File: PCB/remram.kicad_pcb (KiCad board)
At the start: 4 copper layers, 140 x 103 mm, 208 parts, among them J1 4DB-P108-06, J10 70543-0002, J11 Conn_02x13_Odd_Even, J12 70543-0002, J13 70543-0002, J14 70543-0002, J15 70543-0003, J16 62201021121, J17 70543-0001, J18 70543-0001, J19 70543-0001, J2 039531-1002, J20 70543-0003, J21 70543-0003, J22 70543-0003, J23 70543-0003, J3 70543-0002, J4 70543-0002, J5 70543-0002, J6 67068-8000, J7 Conn_02x05, J8 Conn_02x05, J9 70543-0002, Q1 PSMN1R8-40YLC,115, Q2 BUK9840-55, Q3 PSMN1R8-40YLC,115, Q4 BUK9840-55, SW1 OS102011MA1QN1, SW2 PTS645VL39-2, U1 TPS54308, U2 AP2112K-3.3TRG1, U3 ADUM4160, U4 STM32F765VIT6, U5 TMC2130-TA, U6 TMC2130-TA, U7 TMC2130-TA, U8 TMC2130-TA, Y1 TSX-3225 24.0000MF15X-AC3

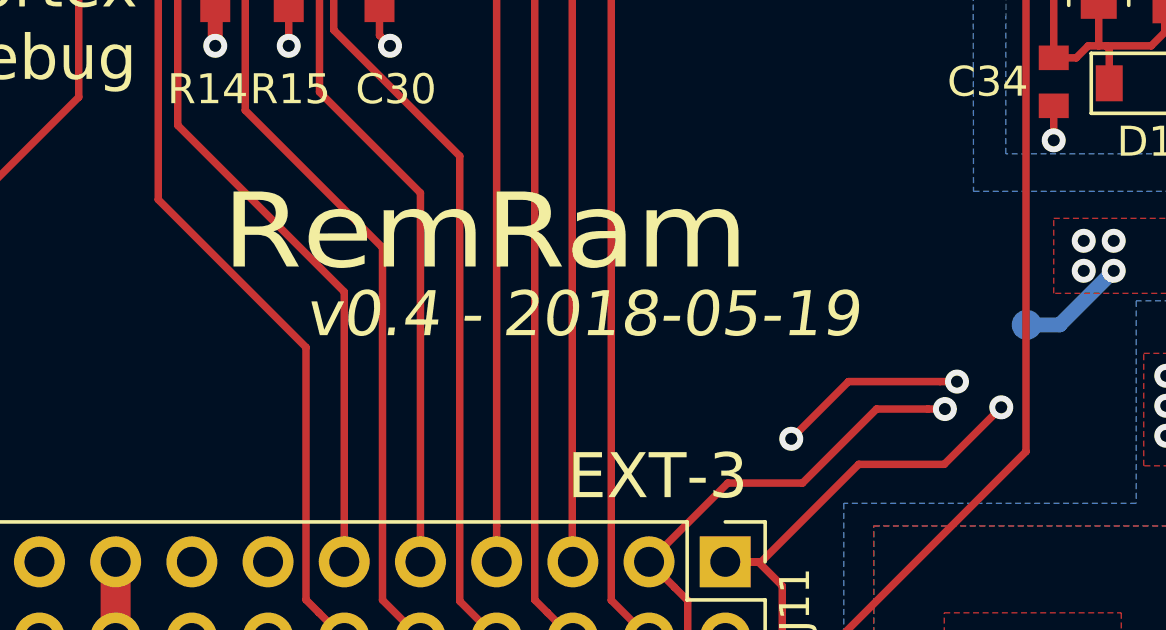
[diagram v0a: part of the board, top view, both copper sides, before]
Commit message: Changed LED to sane values. Updated diodes. v0.5.
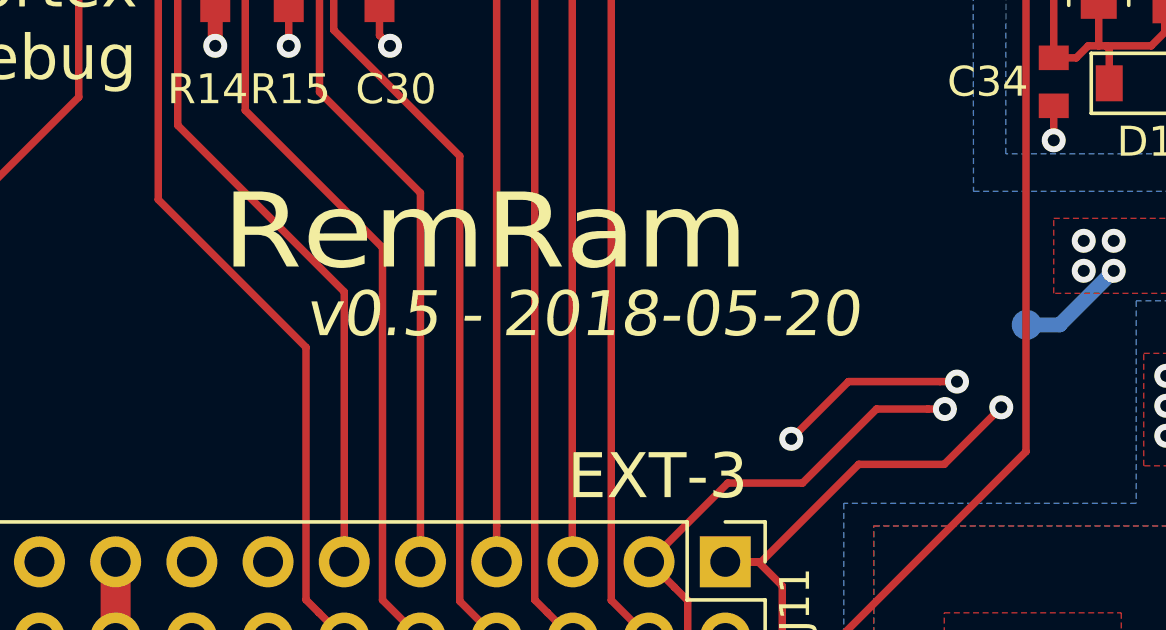
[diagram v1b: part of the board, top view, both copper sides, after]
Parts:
- D5, D7: value SK310A-TP -> SK310A-LTP
- R20, R3: value 68 -> 1k
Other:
- board text added: "v0.5 - 2018-05-20"
- board text removed: "v0.4 - 2018-05-19"
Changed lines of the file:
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@@
       (effects (font (size 1 1) (thickness 0.15)))
     )
-    (fp_text value 68 (at 0 1.45 180) (layer F.Fab)
+    (fp_text value 1k (at 0 1.45 180) (layer F.Fab)
       (effects (font (size 1 1) (thickness 0.15)))
     )
@@
       (effects (font (size 1 1) (thickness 0.15)))
     )
-    (fp_text value SK310A-TP (at 0 2.6 90) (layer F.Fab)
+    (fp_text value SK310A-LTP (at 0 2.6 90) (layer F.Fab)
       (effects (font (size 1 1) (thickness 0.15)))
     )
@@
       (effects (font (size 1 1) (thickness 0.15)))
     )
-    (fp_text value SK310A-TP (at 0 2.6 90) (layer F.Fab)
+    (fp_text value SK310A-LTP (at 0 2.6 90) (layer F.Fab)
       (effects (font (size 1 1) (thickness 0.15)))
     )
@@
       (effects (font (size 1 1) (thickness 0.15)))
     )
-    (fp_text value 68 (at 0 1.45 270) (layer F.Fab)
+    (fp_text value 1k (at 0 1.45 270) (layer F.Fab)
       (effects (font (size 1 1) (thickness 0.15)))
     )
@@
     (arrow2b (pts (xy 202.199068 149.769839) (xy 201.07246 150.356059)))
   )
-  (gr_text "v0.4 - 2018-05-19" (at 134 116) (layer F.SilkS)
+  (gr_text "v0.5 - 2018-05-20" (at 134 116) (layer F.SilkS)
     (effects (font (size 1.5 1.5) (thickness 0.3) italic))
   )

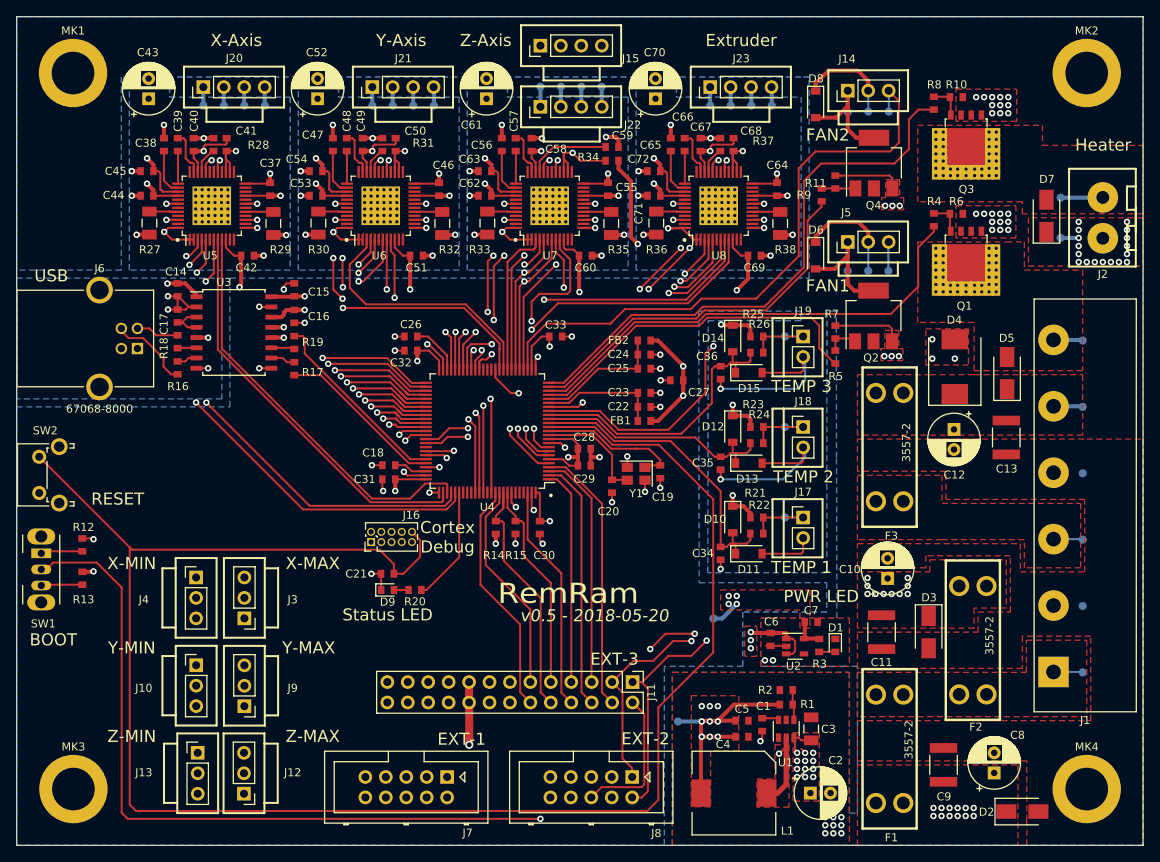
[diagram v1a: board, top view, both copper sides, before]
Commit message: Added a battery for SRAM backup.
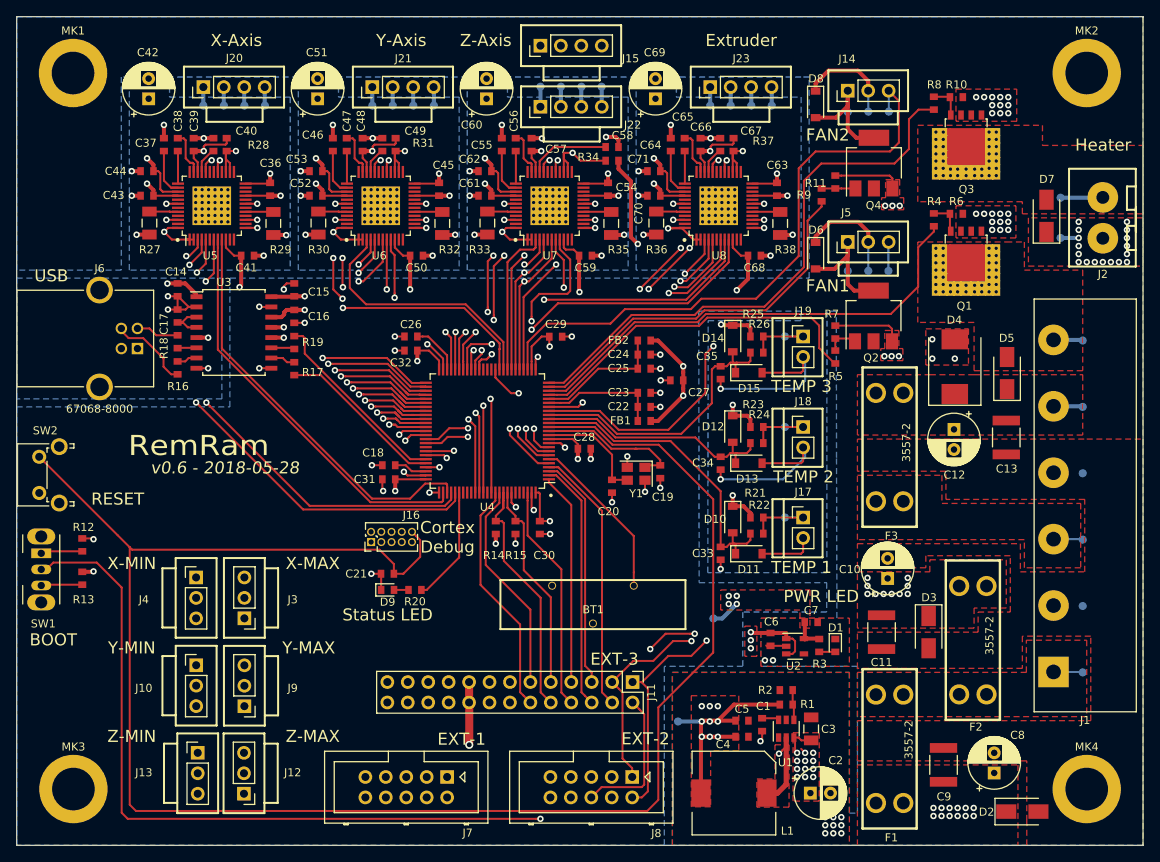
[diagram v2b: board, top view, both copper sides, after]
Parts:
- removed the C33 at (129.2, 81.3)
- added BT1: VBH2032-1, custom-footprints:VBH2032-1, F.Cu at (133.8, 114.2)
- moved C29 16.4 mm to (129.2, 81.3)
- renumbered C34 to C33, C35 to C34, C36 to C35, C37 to C36, C38 to C37, C39 to C38, C40 to C39, C41 to C40, C42 to C41, C43 to C42, C44 to C43, C45 to C44, C46 to C45, C47 to C46, C48 to C47, C49 to C48, C50 to C49, C51 to C50, C52 to C51, C53 to C52, C54 to C53, C55 to C54, C56 to C55, C57 to C56, C58 to C57, C59 to C58, C60 to C59, C61 to C60, C62 to C61, C63 to C62, C64 to C63, C65 to C64, C66 to C65, C67 to C66, C68 to C67, C69 to C68, C70 to C69, C71 to C70, C72 to C71
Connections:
- U4 pad 6: VDD3V3 -> Net-(BT1-Pad2)
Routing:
- net Net-(BT1-Pad2): track 0.00 -> 30.8 mm
- net VDD3V3: track 117.7 -> 111.6 mm
- net GND: track 223.3 -> 221.3 mm
- net /MCU/SS_SD: track 71.3 -> 72.2 mm
- net /MCU/EXT_D4: track 26.9 -> 26.4 mm
- net /MCU/EXT_D2: track 29.5 -> 29.0 mm
- net /MCU/EXT_D1: track 33.7 -> 33.2 mm
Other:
- board text added: "v0.6 - 2018-05-28"
- board text removed: "v0.5 - 2018-05-20"

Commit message: Version 0.7
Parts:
- Q1, Q3: value PSMN1R8-40YLC,115 -> PSMN1R2-30YLC,115
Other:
- board text added: "v0.7 - 2018-05-28"
- board text removed: "v0.6 - 2018-05-28"

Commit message: Final version that goes to the lab.
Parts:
- J16: footprint Connector_PinHeader_1.27mm:PinHeader_2x05_P1.27mm_Vertical -> custom-footprints:PinHeader_2x05_P1.27mm_Vertical

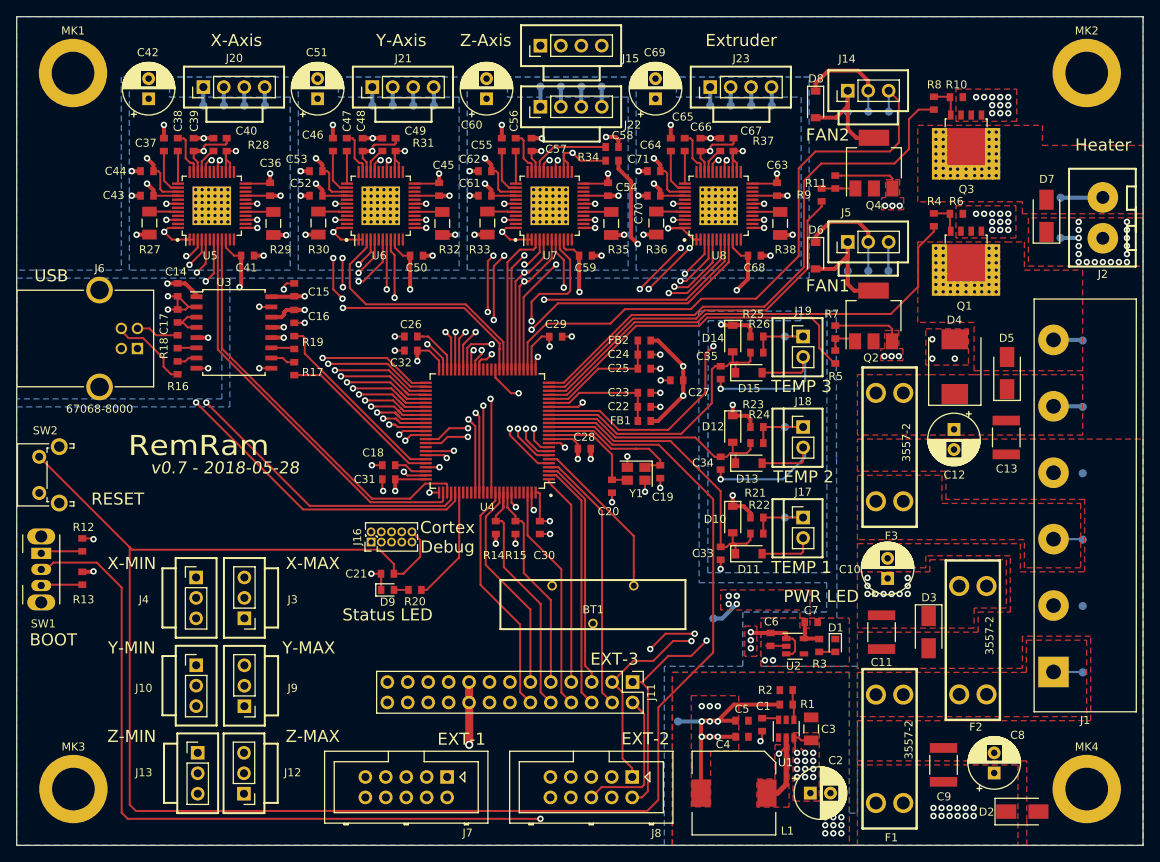
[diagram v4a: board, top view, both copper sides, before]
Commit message: Change some traces and silkscreen text.
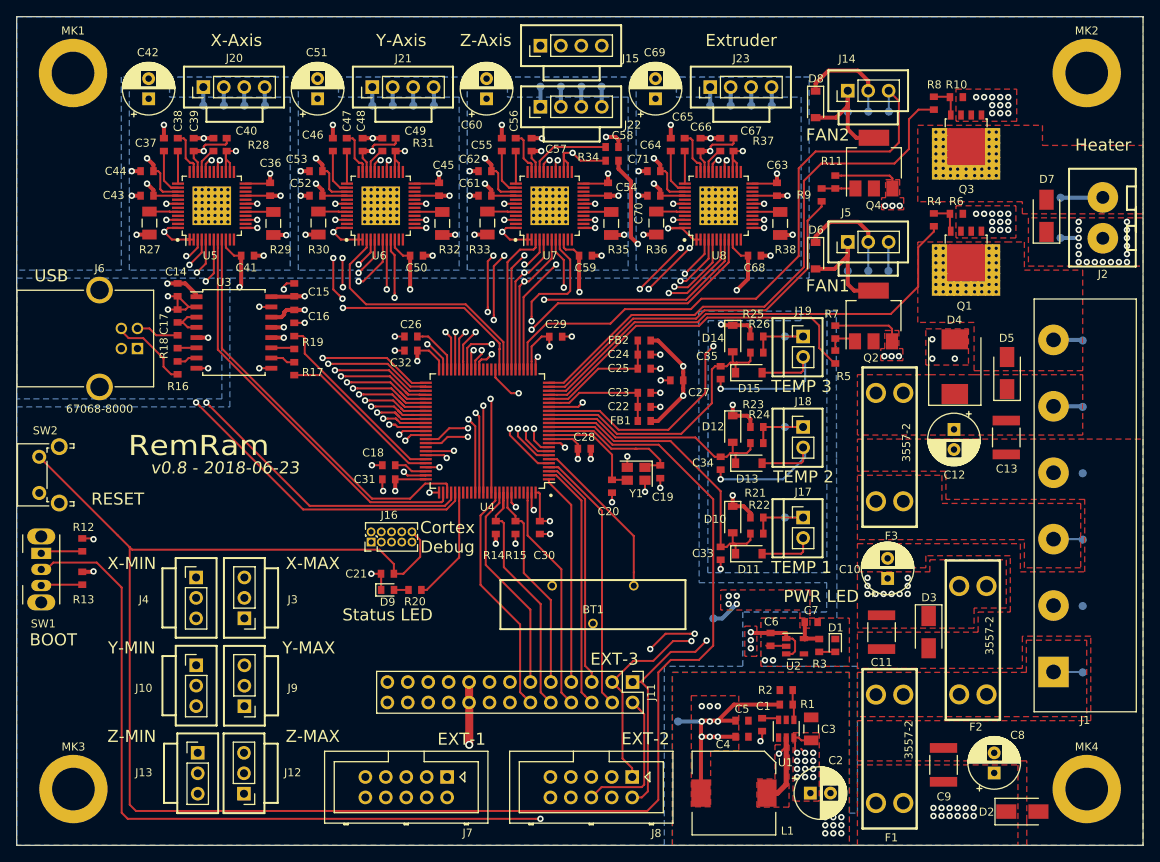
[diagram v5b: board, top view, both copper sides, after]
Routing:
- net /MCU/nRESET: track 221.9 -> 224.0 mm
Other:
- board text added: "v0.8 - 2018-06-23"
- board text removed: "v0.7 - 2018-05-28"
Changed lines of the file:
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@@
     (thickness 1.6)
     (drawings 45)
-    (tracks 2011)
+    (tracks 2013)
     (zones 0)
     (modules 208)
@@
     (descr "Through hole straight pin header, 2x05, 1.27mm pitch, double rows")
     (tags "Through hole pin header THT 2x05 1.27mm double row")
-    (fp_text reference J16 (at 0.635 -1.695 90) (layer F.SilkS)
+    (fp_text reference J16 (at 3.35 2.25 180) (layer F.SilkS)
       (effects (font (size 1 1) (thickness 0.15)))
     )
@@
     (tags resistor)
     (attr smd)
-    (fp_text reference R11 (at 0.15 2.45) (layer F.SilkS)
+    (fp_text reference R11 (at -2.6 0.45) (layer F.SilkS)
       (effects (font (size 1 1) (thickness 0.15)))
     )
@@
     (tags resistor)
     (attr smd)
-    (fp_text reference R5 (at 2.4 -0.05) (layer F.SilkS)
+    (fp_text reference R5 (at 2.4 -1.05) (layer F.SilkS)
       (effects (font (size 1 1) (thickness 0.15)))
     )
@@
     (arrow2b (pts (xy 202.199068 149.769839) (xy 201.07246 150.356059)))
   )
-  (gr_text "v0.7 - 2018-05-28" (at 88.075 97.625) (layer F.SilkS)
+  (gr_text "v0.8 - 2018-06-23" (at 88.075 97.625) (layer F.SilkS)
     (effects (font (size 1.5 1.5) (thickness 0.3) italic))
   )
@@
   (segment (start 76.55 107.8) (end 76.25 107.5) (width 0.25) (layer F.Cu) (net 65))
   (segment (start 109.082727 110.790025) (end 109.082727 109.582727) (width 0.25) (layer F.Cu) (net 65))
+  (segment (start 134.040767 92.55) (end 129.35 92.55) (width 0.25) (layer F.Cu) (net 65))
   (segment (start 136.2408 94.750033) (end 134.040767 92.55) (width 0.25) (layer F.Cu) (net 65))
   (segment (start 142.000033 94.750033) (end 136.2408 94.750033) (width 0.25) (layer F.Cu) (net 65))
-  (segment (start 134.040767 92.55) (end 129.35 92.55) (width 0.25) (layer F.Cu) (net 65))
-  (segment (start 148.775002 120.574998) (end 148.775002 101.525002) (width 0.25) (layer F.Cu) (net 65))
-  (segment (start 141.95 127.4) (end 148.775002 120.574998) (width 0.25) (layer F.Cu) (net 65))
-  (segment (start 148.775002 101.525002) (end 142.000033 94.750033) (width 0.25) (layer F.Cu) (net 65))
-  (segment (start 77.024998 140.274998) (end 140.575002 140.274998) (width 0.25) (layer F.Cu) (net 65))
-  (segment (start 76.25 139.5) (end 77.024998 140.274998) (width 0.25) (layer F.Cu) (net 65))
   (segment (start 129.35 92.55) (end 128.35 92.55) (width 0.25) (layer F.Cu) (net 65))
-  (segment (start 140.575002 140.274998) (end 141.95 138.9) (width 0.25) (layer F.Cu) (net 65))
+  (segment (start 148.775002 119.724998) (end 148.775002 101.525002) (width 0.25) (layer F.Cu) (net 65))
+  (segment (start 147 121.5) (end 148.775002 119.724998) (width 0.25) (layer F.Cu) (net 65))
+  (segment (start 143.5 121.5) (end 147 121.5) (width 0.25) (layer F.Cu) (net 65))
   (segment (start 76.25 107.5) (end 76.25 139.5) (width 0.25) (layer F.Cu) (net 65))
-  (segment (start 141.95 138.9) (end 141.95 127.4) (width 0.25) (layer F.Cu) (net 65))
+  (segment (start 76.25 139.5) (end 77.024998 140.274998) (width 0.25) (layer F.Cu) (net 65))
+  (segment (start 77.024998 140.274998) (end 140.575002 140.274998) (width 0.25) (layer F.Cu) (net 65))
+  (segment (start 140.575002 140.274998) (end 141.95 138.9) (width 0.25) (layer F.Cu) (net 65))
+  (segment (start 141.95 138.9) (end 141.95 123.05) (width 0.25) (layer F.Cu) (net 65))
+  (segment (start 148.775002 101.525002) (end 142.000033 94.750033) (width 0.25) (layer F.Cu) (net 65))
+  (segment (start 141.95 123.05) (end 143.5 121.5) (width 0.25) (layer F.Cu) (net 65))
   (via (at 114.75 97.55) (size 0.8) (drill 0.4) (layers F.Cu B.Cu) (net 66))
   (segment (start 107.52 105.58) (end 107.52 104.78) (width 0.25) (layer In1.Cu) (net 66) (status 10))
@@
   (segment (start 138.7 138.59) (end 139.902081 138.59) (width 0.25) (layer F.Cu) (net 70))
   (segment (start 140.650011 137.84207) (end 140.650011 125.050011) (width 0.25) (layer F.Cu) (net 70))
-  (via (at 147.95 119.1) (size 0.8) (drill 0.4) (layers F.Cu B.Cu) (net 70))
-  (segment (start 146.05 121) (end 147.95 119.1) (width 0.25) (layer F.Cu) (net 70))
-  (segment (start 143.2 121) (end 146.05 121) (width 0.25) (layer F.Cu) (net 70))
-  (segment (start 139.95 124.25) (end 143.2 121) (width 0.25) (layer F.Cu) (net 70))
-  (segment (start 138.75 124.25) (end 139.95 124.25) (width 0.25) (layer F.Cu) (net 70))
   (via (at 129.25 72.349998) (size 0.8) (drill 0.4) (layers F.Cu B.Cu) (net 70))
   (segment (start 125.300002 72.35) (end 129.249998 72.35) (width 0.25) (layer In1.Cu) (net 70))
@@
   (segment (start 148.2 71.623004) (end 145.423008 74.399996) (width 0.25) (layer F.Cu) (net 70))
   (segment (start 148.2 69.25) (end 148.2 71.623004) (width 0.25) (layer F.Cu) (net 70))
-  (segment (start 147.2 76.899996) (end 145.099999 74.799995) (width 0.25) (layer In1.Cu) (net 70))
+  (via (at 147.95 119.1) (size 0.8) (drill 0.4) (layers F.Cu B.Cu) (net 70))
+  (segment (start 147.95 119.1) (end 147.2 118.35) (width 0.25) (layer In1.Cu) (net 70))
   (segment (start 145.099999 74.799995) (end 144.7 74.399996) (width 0.25) (layer In1.Cu) (net 70))
+  (segment (start 147.2 76.899996) (end 145.099999 74.799995) (width 0.25) (layer In1.Cu) (net 70))
   (segment (start 147.2 118.35) (end 147.2 76.899996) (width 0.25) (layer In1.Cu) (net 70))
-  (segment (start 147.95 119.1) (end 147.2 118.35) (width 0.25) (layer In1.Cu) (net 70))
+  (segment (start 146.55 120.5) (end 147.95 119.1) (width 0.25) (layer F.Cu) (net 70))
+  (segment (start 143.5 120.5) (end 146.55 120.5) (width 0.25) (layer F.Cu) (net 70))
+  (segment (start 138.75 124.25) (end 139.75 124.25) (width 0.25) (layer F.Cu) (net 70))
+  (segment (start 139.75 124.25) (end 143.5 120.5) (width 0.25) (layer F.Cu) (net 70))
   (segment (start 123.649998 88.349998) (end 124.034315 88.349998) (width 0.25) (layer F.Cu) (net 71))
   (segment (start 124.034315 88.349998) (end 124.6 88.349998) (width 0.25) (layer F.Cu) (net 71))
